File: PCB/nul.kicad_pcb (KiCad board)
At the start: 2 copper layers, 10 x 40 mm, 33 parts, among them J2 LED Socket, U1 ESP32-C3FH4, U2 AMS1117-3.3, U3 SN74AHCT1G125DBVR, U4 XRCGB40M000F1S1DR0, U5 SRV05-4

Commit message: some wiring
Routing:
- net Net-(USBC1-CC2): track 0.00 -> 9.74 mm
- net USB_D-: track 0.00 -> 7.26 mm, vias 0 -> 1
- net USB_D+: track 0.00 -> 5.75 mm
- net Net-(USBC1-CC1): track 0.00 -> 4.72 mm
- added copper zone on B.Cu, net GND
- added copper zone on F.Cu, net GND

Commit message: pcb v1
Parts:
- removed C1: 0.1uF ceramic, Capacitor_SMD:C_0402_1005Metric
- moved R3 0.10 mm to (120.0, 70.1)
- turned R1 to 90 degrees
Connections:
- net Net-(U1-GPIO18/USB_D-) renamed /USB_DATA+
- net Net-(U1-GPIO19/USB_D+) renamed /USB_DATA-
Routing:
- net +3.3V: track 0.00 -> 75.9 mm, vias 0 -> 6
- net GND: track 0.00 -> 68.9 mm, vias 0 -> 19
- net +5V: track 0.00 -> 57.3 mm, vias 0 -> 2
- net /USB_DATA-: track 0.00 -> 16.0 mm, vias 0 -> 2
- net LED: track 0.00 -> 15.9 mm
- net Net-(U1-LNA_IN): track 0.00 -> 14.5 mm, vias 0 -> 2
- net /USB_DATA+: track 0.00 -> 14.3 mm
- net Net-(U1-XTAL_P): track 0.00 -> 9.46 mm, vias 0 -> 2
- net Net-(U1-XTAL_N): track 0.00 -> 9.34 mm, vias 0 -> 2
- net Net-(U3-VCC): track 0.00 -> 5.50 mm
- net Net-(JP2-SIG): track 0.00 -> 4.60 mm
- net Net-(U1-CHIP_EN): track 0.00 -> 4.00 mm
- net Net-(U3-Y): track 0.00 -> 3.01 mm
- net Net-(U1-VDD_SPI): track 0.00 -> 2.75 mm
- net Net-(J2-Pin_2): track 0.00 -> 2.75 mm
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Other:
- board size 10 x 40 mm -> 11.1 x 40 mm

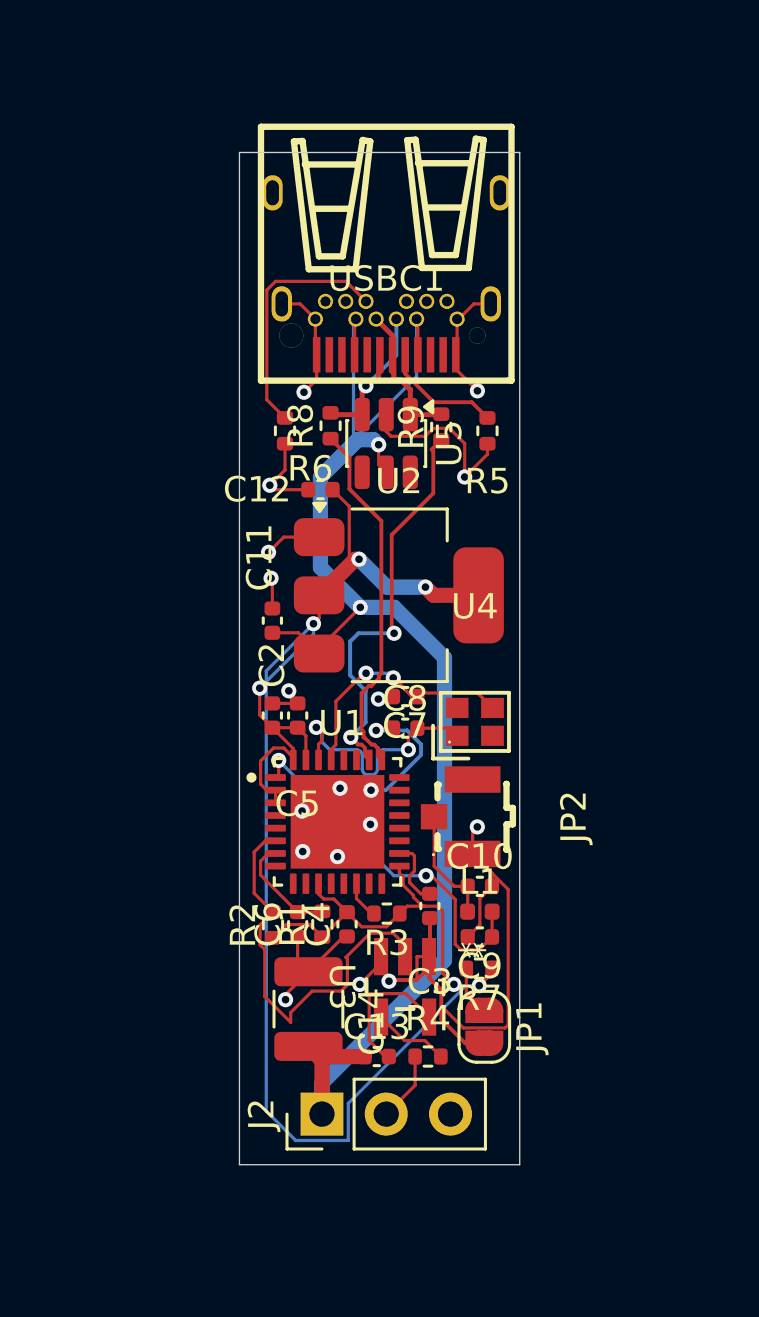
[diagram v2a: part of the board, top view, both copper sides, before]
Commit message: add silkscreen art and round corners
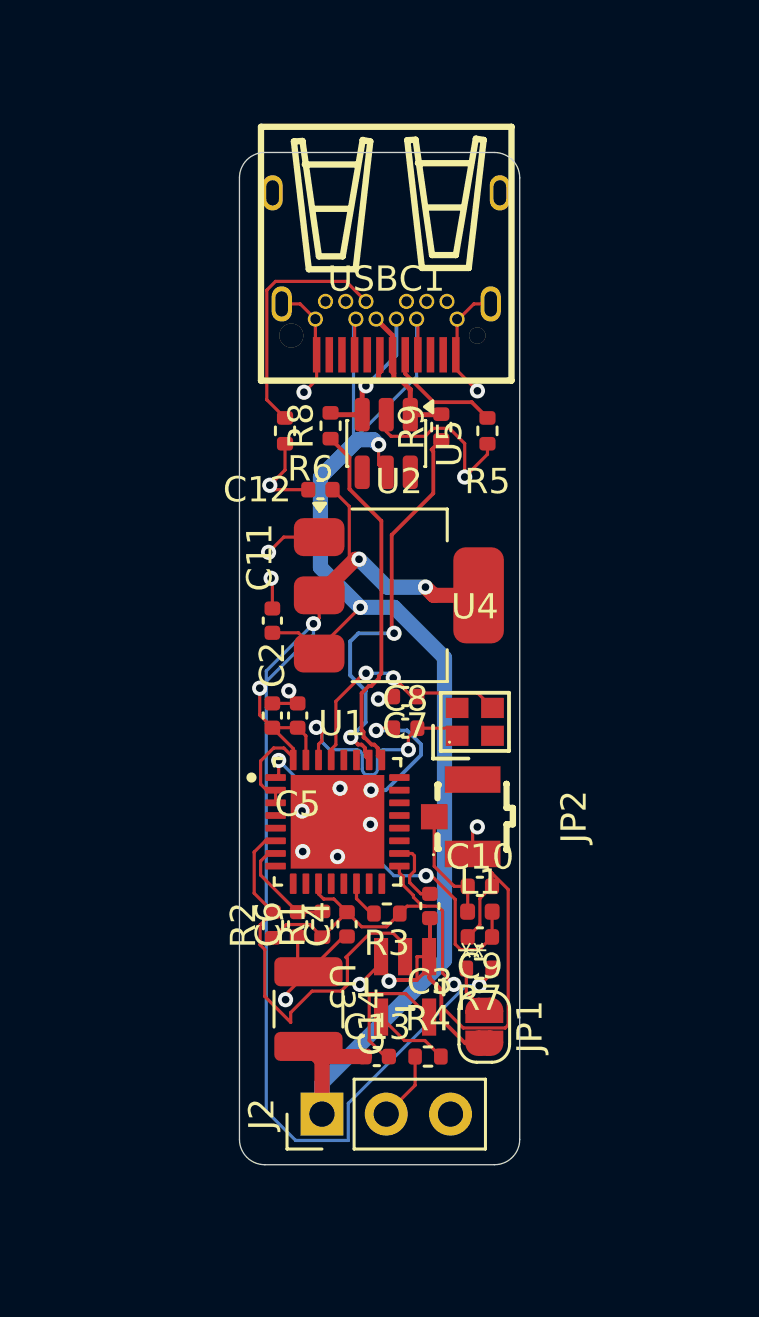
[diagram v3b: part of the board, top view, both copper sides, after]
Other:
- outline, holes or cut-outs redrawn
- board text added: "Ginobeano"
- board text added: "nul"

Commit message: feat: update PCB
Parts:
- removed JP1: SolderJumper_2_Open, Jumper:SolderJumper-2_P1.3mm_Open_RoundedPad1.0x1.5mm
- removed R7: 10k, Resistor_SMD:R_0402_1005Metric
- moved L1 8.49 mm to (115.7, 67.2), turned to -90 degrees
- moved C9 8.25 mm to (115.7, 69.0), turned to -90 degrees
- moved C10 8.22 mm to (116.2, 65.8)
- moved JP2 6.82 mm to (116.6, 63.2)
- moved C5 5.06 mm to (120.2, 65.7)
- moved C2 4.58 mm to (119.2, 65.0)
- moved U3 4.08 mm to (122.3, 76.7)
- moved C3 4.04 mm to (123.2, 73.5)
- moved C4 4.04 mm to (120.0, 74.2)
- moved C6 4.04 mm to (118.0, 74.2)
- moved R1 4.04 mm to (119.0, 74.2)
- moved R2 4.04 mm to (117.0, 74.3)
- moved R3 4.04 mm to (121.5, 73.8)
- moved U1 4.04 mm to (119.6, 70.2)
- moved C13 3.75 mm to (119.6, 79.5)
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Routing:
- net +5V: track 57.3 -> 25.5 mm, vias 2 -> 11
- net GND: track 68.9 -> 55.5 mm, vias 19 -> 21
- net Net-(U1-LNA_IN): track 14.5 -> 2.34 mm, vias 2 -> 0
- net /USB_DATA+: track 14.3 -> 21.6 mm, vias 0 -> 2
- net USB_D-: track 6.57 -> 11.5 mm, vias 1 -> 2
- net Net-(U1-XTAL_N): track 9.34 -> 13.8 mm
- net /USB_DATA-: track 16.0 -> 18.3 mm, vias 2 -> 0
- net Net-(JP1-A): track 1.94 -> 0.00 mm
- net LED: track 15.9 -> 14.3 mm, vias 0 -> 2
- net Net-(U1-XTAL_P): track 9.46 -> 8.26 mm
- net Net-(U3-Y): track 3.01 -> 1.88 mm
- net +3.3V: track 75.9 -> 76.9 mm, vias 6 -> 7
- net Net-(JP2-SIG): track 4.60 -> 3.53 mm
- added copper zone on In2.Cu, net +5V
- added copper zone on In1.Cu, net GND
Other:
- board size 11.1 x 40 mm -> 11 x 43.2 mm
- copper layers 2 -> 4

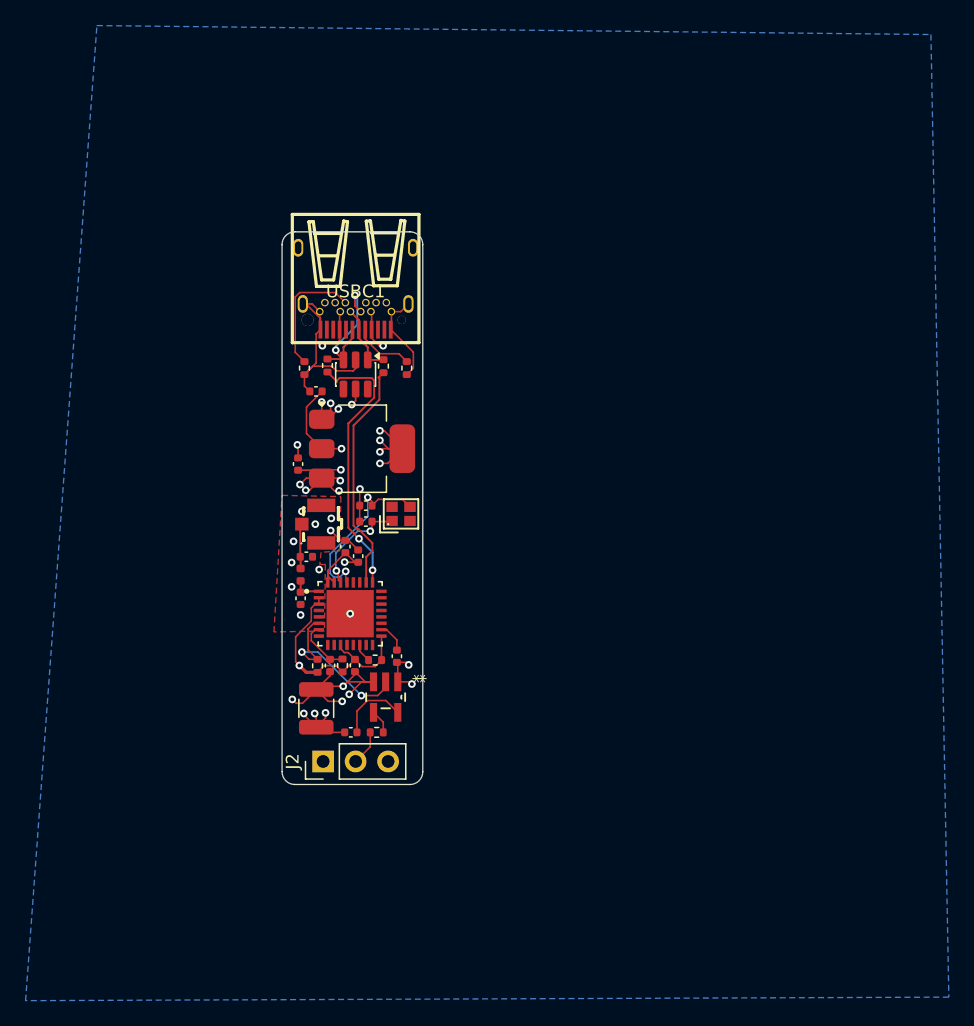
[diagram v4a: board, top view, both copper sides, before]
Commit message: fix: ground fill and ldo output trace
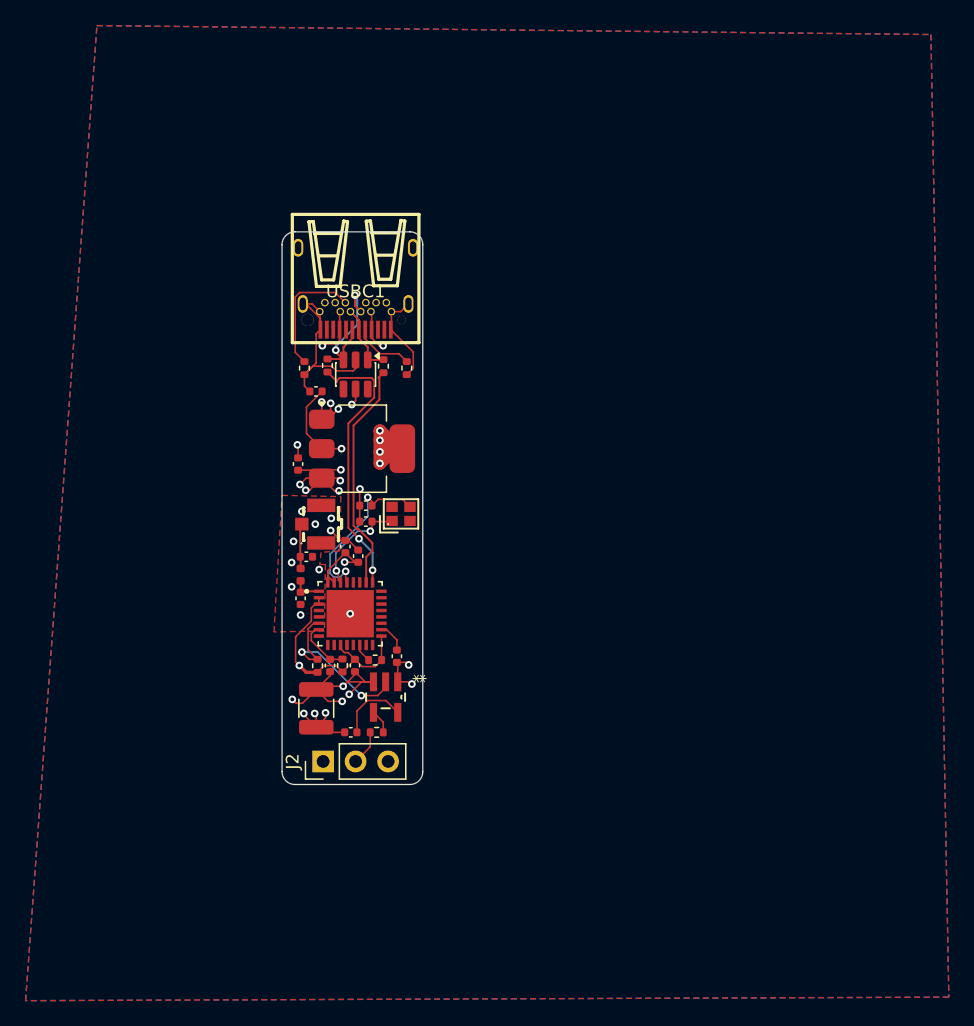
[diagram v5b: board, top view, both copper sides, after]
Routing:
- net +3.3V: track 76.9 -> 79.5 mm
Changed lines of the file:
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@@
 		(start 122.15 57.3)
 		(end 121.9 57.55)
-		(width 0.127)
+		(width 1)
+		(layer "F.Cu")
+		(net "+3.3V")
+	)
+	(segment
+		(start 123.05 57.3)
+		(end 121.9 58.45)
+		(width 1)
 		(layer "F.Cu")
 		(net "+3.3V")
@@
 	)
 	(segment
-		(start 122.25 55.9)
-		(end 121.9 55.9)
-		(width 0.127)
-		(layer "F.Cu")
-		(net "+3.3V")
-	)
-	(segment
 		(start 117.025 74.785)
 		(end 116.135 74.785)
@@
 	)
 	(segment
+		(start 123.65 57.3)
+		(end 123.3 57.3)
+		(width 1)
+		(layer "F.Cu")
+		(net "+3.3V")
+	)
+	(segment
 		(start 118.975 74.76)
 		(end 118.975 74.745)
@@
 	)
 	(segment
+		(start 121.9 55.9)
+		(end 121.9 58.45)
+		(width 1)
+		(layer "F.Cu")
+		(net "+3.3V")
+	)
+	(segment
 		(start 121.5245 74.3355)
 		(end 122.035 73.825)
@@
 	)
 	(segment
+		(start 116.5345 69.754928)
+		(end 116.5345 70.78129)
+		(width 0.127)
+		(layer "F.Cu")
+		(net "+3.3V")
+	)
+	(segment
+		(start 116.1595 54.0455)
+		(end 116.1595 56.1095)
+		(width 0.127)
+		(layer "F.Cu")
+		(net "+3.3V")
+	)
+	(segment
+		(start 120.5155 74.3355)
+		(end 121.5245 74.3355)
+		(width 0.127)
+		(layer "F.Cu")
+		(net "+3.3V")
+	)
+	(segment
+		(start 118.4745 74.2595)
+		(end 117.5505 74.2595)
+		(width 0.127)
+		(layer "F.Cu")
+		(net "+3.3V")
+	)
+	(segment
+		(start 117.35 57.3)
+		(end 118.9 57.3)
+		(width 0.127)
+		(layer "F.Cu")
+		(net "+3.3V")
+	)
+	(segment
+		(start 118.476328 66.153672)
+		(end 119.2 65.43)
+		(width 0.127)
+		(layer "F.Cu")
+		(net "+3.3V")
+	)
+	(segment
+		(start 123.65 57.3)
+		(end 122.55 57.3)
+		(width 1)
+		(layer "F.Cu")
+		(net "+3.3V")
+	)
+	(segment
+		(start 118.975 74.745)
+		(end 119.95 73.77)
+		(width 0.127)
+		(layer "F.Cu")
+		(net "+3.3V")
+	)
+	(segment
+		(start 117.13 68.95)
+		(end 117.13 69.45)
+		(width 0.127)
+		(layer "F.Cu")
+		(net "+3.3V")
+	)
+	(segment
+		(start 117.825 67.255)
+		(end 118.325 67.755)
+		(width 0.127)
+		(layer "F.Cu")
+		(net "+3.3V")
+	)
+	(segment
+		(start 117.825 66.831328)
+		(end 117.825 67.755)
+		(width 0.127)
+		(layer "F.Cu")
+		(net "+3.3V")
+	)
+	(segment
+		(start 116.1595 56.1095)
+		(end 117.35 57.3)
+		(width 0.127)
+		(layer "F.Cu")
+		(net "+3.3V")
+	)
+	(segment
+		(start 115.3095 73.9595)
+		(end 115.6 74.25)
+		(width 0.127)
+		(layer "F.Cu")
+		(net "+3.3V")
+	)
+	(segment
+		(start 118.476328 66.18)
+		(end 117.825 66.831328)
+		(width 0.127)
+		(layer "F.Cu")
+		(net "+3.3V")
+	)
+	(segment
+		(start 123.3 57.3)
+		(end 121.9 55.9)
+		(width 1)
+		(layer "F.Cu")
+		(net "+3.3V")
+	)
+	(segment
+		(start 116.839428 69.45)
+		(end 116.5345 69.754928)
+		(width 0.127)
+		(layer "F.Cu")
+		(net "+3.3V")
+	)
+	(segment
+		(start 117.38 52.825)
+		(end 116.1595 54.0455)
+		(width 0.127)
+		(layer "F.Cu")
+		(net "+3.3V")
+	)
+	(segment
+		(start 122.55 57.3)
+		(end 121.9 56.65)
+		(width 1)
+		(layer "F.Cu")
+		(net "+3.3V")
+	)
+	(segment
+		(start 119.95 73.77)
+		(end 120.5155 74.3355)
+		(width 0.127)
+		(layer "F.Cu")
+		(net "+3.3V")
+	)
+	(segment
 		(start 123.65 57.3)
 		(end 122.15 57.3)
-		(width 0.127)
-		(layer "F.Cu")
-		(net "+3.3V")
-	)
-	(segment
-		(start 116.5345 69.754928)
-		(end 116.5345 70.78129)
-		(width 0.127)
-		(layer "F.Cu")
-		(net "+3.3V")
-	)
-	(segment
-		(start 116.1595 54.0455)
-		(end 116.1595 56.1095)
-		(width 0.127)
-		(layer "F.Cu")
-		(net "+3.3V")
-	)
-	(segment
-		(start 120.5155 74.3355)
-		(end 121.5245 74.3355)
-		(width 0.127)
-		(layer "F.Cu")
-		(net "+3.3V")
-	)
-	(segment
-		(start 118.4745 74.2595)
-		(end 117.5505 74.2595)
-		(width 0.127)
-		(layer "F.Cu")
-		(net "+3.3V")
-	)
-	(segment
-		(start 123.65 57.3)
-		(end 122.5 58.45)
-		(width 0.127)
-		(layer "F.Cu")
-		(net "+3.3V")
-	)
-	(segment
-		(start 117.35 57.3)
-		(end 118.9 57.3)
-		(width 0.127)
-		(layer "F.Cu")
-		(net "+3.3V")
-	)
-	(segment
-		(start 118.476328 66.153672)
-		(end 119.2 65.43)
-		(width 0.127)
-		(layer "F.Cu")
-		(net "+3.3V")
-	)
-	(segment
-		(start 118.975 74.745)
-		(end 119.95 73.77)
-		(width 0.127)
-		(layer "F.Cu")
-		(net "+3.3V")
-	)
-	(segment
-		(start 122.5 58.45)
-		(end 121.9 58.45)
-		(width 0.127)
-		(layer "F.Cu")
-		(net "+3.3V")
-	)
-	(segment
-		(start 117.13 68.95)
-		(end 117.13 69.45)
-		(width 0.127)
-		(layer "F.Cu")
-		(net "+3.3V")
-	)
-	(segment
-		(start 117.825 67.255)
-		(end 118.325 67.755)
-		(width 0.127)
-		(layer "F.Cu")
-		(net "+3.3V")
-	)
-	(segment
-		(start 117.825 66.831328)
-		(end 117.825 67.755)
-		(width 0.127)
-		(layer "F.Cu")
-		(net "+3.3V")
-	)
-	(segment
-		(start 116.1595 56.1095)
-		(end 117.35 57.3)
-		(width 0.127)
-		(layer "F.Cu")
-		(net "+3.3V")
-	)
-	(segment
-		(start 115.3095 73.9595)
-		(end 115.6 74.25)
-		(width 0.127)
-		(layer "F.Cu")
-		(net "+3.3V")
-	)
-	(segment
-		(start 118.476328 66.18)
-		(end 117.825 66.831328)
-		(width 0.127)
-		(layer "F.Cu")
-		(net "+3.3V")
-	)
-	(segment
-		(start 116.839428 69.45)
-		(end 116.5345 69.754928)
-		(width 0.127)
-		(layer "F.Cu")
-		(net "+3.3V")
-	)
-	(segment
-		(start 117.38 52.825)
-		(end 116.1595 54.0455)
-		(width 0.127)
-		(layer "F.Cu")
-		(net "+3.3V")
-	)
-	(segment
-		(start 119.95 73.77)
-		(end 120.5155 74.3355)
-		(width 0.127)
+		(width 1)
 		(layer "F.Cu")
 		(net "+3.3V")
@@
 	)
 	(segment
-		(start 122.55 57.3)
-		(end 121.9 56.65)
-		(width 0.127)
-		(layer "F.Cu")
-		(net "+3.3V")
-	)
-	(segment
-		(start 123.65 57.3)
-		(end 122.25 55.9)
-		(width 0.127)
-		(layer "F.Cu")
-		(net "+3.3V")
-	)
-	(segment
 		(start 118.476328 66.18)
 		(end 118.476328 66.153672)
@@
 	)
 	(segment
+		(start 123.65 57.3)
+		(end 123.05 57.3)
+		(width 1)
+		(layer "F.Cu")
+		(net "+3.3V")
+	)
+	(segment
 		(start 119.2 65.43)
 		(end 119.95 66.18)
-		(width 0.127)
-		(layer "F.Cu")
-		(net "+3.3V")
-	)
-	(segment
-		(start 123.65 57.3)
-		(end 122.55 57.3)
 		(width 0.127)
 		(layer "F.Cu")
@@
 	(zone
 		(net "GND")
-		(layers "B.Cu" "In1.Cu")
+		(layers "F.Cu" "B.Cu" "In1.Cu")
 		(hatch edge 0.5)
 		(connect_pads
